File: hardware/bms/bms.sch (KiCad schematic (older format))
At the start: 185 parts

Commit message: fixed power schematics
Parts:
- removed L?: 4.7uH, Inductor_SMD:L_0805_2012Metric, symbol pspice:INDUCTOR
- removed R? (x2): R_Small, Resistor_SMD:R_0603_1608Metric_Pad1.05x0.95mm_HandSolder, symbol Device:R_Small
- added R?: 412K, Resistor_SMD:R_1210_3225Metric_Pad1.42x2.65mm_HandSolder, symbol Device:R
- added R?: 200K, Resistor_SMD:R_1210_3225Metric_Pad1.42x2.65mm_HandSolder, symbol Device:R
- C?: value CAP -> 2.2uF
- C? (x2): value C -> 100nF
- C?: value CP1 -> 22uF
- C?: value C -> 2.2uF
- C? (x2): value C -> 2.2nF
- C?: value C -> 100pF
- C?: value C -> 47uF
- L?: value 47uH -> 68uH
- R?: value 100K -> 82.5K
- R?: value R_Small -> 562K
- R?: value R_Small -> 174K
- R?: value R_Small -> 100K
- U?: value TPS560430 -> TPS560430x3F
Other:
- moved on the sheet: C?, D?, L?, Q?, R?

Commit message: Added On/Off control button
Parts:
- removed C?: 47uF, Capacitor_SMD:C_0603_1608Metric_Pad1.05x0.95mm_HandSolder, symbol Device:C
- removed J? (x4): Conn_01x02, symbol BMS:Conn_01x02
- removed JP?: PackLoad+, symbol BMS:JUMPER
- added C?: 47uF, Capacitor_Tantalum_SMD:CP_EIA-3528-21_Kemet-B, symbol Device:CP1
- added C?: 0.1uF, Capacitor_SMD:C_0603_1608Metric_Pad1.05x0.95mm_HandSolder, symbol Device:C
- added J? (x2): Conn_01x03, symbol Connector_Generic:Conn_01x03
- added JP?: Load On/Off, symbol BMS:JUMPER
- added R?: 10K, Resistor_SMD:R_0603_1608Metric_Pad1.05x0.95mm_HandSolder, symbol Device:R_Small
- added SW?: On/Off, symbol Switch:SW_Push
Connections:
- wire segments 657 -> 666
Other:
- note added: "Pack charging"
- note added: "Pack discharging"
- note added: "Series stacking connectors"
- moved on the sheet: C?, J?, JP?, R?

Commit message: added required provisions
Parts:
- removed J?: Conn_01x06, symbol BMS:Conn_01x06
- removed SW?: On/Off, symbol Switch:SW_Push
- added J?: Conn_01x08, symbol Connector_Generic:Conn_01x08
- added JP?: WakeUp, symbol BMS:JUMPER
- added R? (x4): 10K, Resistor_SMD:R_0603_1608Metric_Pad1.05x0.95mm_HandSolder, symbol Device:R_Small
- added R?: 20K, Resistor_SMD:R_0603_1608Metric_Pad1.05x0.95mm_HandSolder, symbol Device:R_Small
- added SW?: SW_DIP_x03, symbol Switch:SW_DIP_x03
- JP?: value Load On/Off -> Load_On/Off
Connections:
- net labels added: ADC, CFG_ID
- net labels removed: PACK_ID
- wire segments 666 -> 690
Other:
- note added: "CFG_ID ADC"
- note added: "Note: LM5164DDAR has limit of 100V input\nin case the pack voltage exceeds 100V then \na provision is provided with external 5V (+5VF) input\nto wakeup the stm32 if it is powered down due to\nlow Battery"
- note added: "Note:\n1) Load_On/Off is of 10A 100VDC rating\n2) Load_On/Off and wakeup connector \n connects to a panel mounted DPDT switch"
- note removed: "PACK ID ADC"
- moved on the sheet: J?, JP?, R?

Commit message: added bypass link for 3V3 power
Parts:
- added JP?: PWR_3V3_ON, symbol BMS:JUMPER
- JP? (x6): symbol bms-rescue:JUMPER-BMS -> bms-rescue:JUMPER-BMS-bms-rescue
- Q? (x5): symbol bms-rescue:Q_PMOS_GSD-BMS -> bms-rescue:Q_PMOS_GSD-BMS-bms-rescue
- U?: symbol bms-rescue:LSI94202-BMS -> bms-rescue:LSI94202-BMS-bms-rescue
- U?: symbol bms-rescue:TPS560430-BMS -> bms-rescue:TPS560430-BMS-bms-rescue
- U?: symbol bms-rescue:USBLC6-2SC6-BMS -> bms-rescue:USBLC6-2SC6-BMS-bms-rescue
- Y?: symbol bms-rescue:Crystal-BMS -> bms-rescue:Crystal-BMS-bms-rescue
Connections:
- wire segments 690 -> 691
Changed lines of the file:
@@
 $EndDescr
 $Comp
-L bms-rescue:LSI94202-BMS U?
+L bms-rescue:LSI94202-BMS-bms-rescue U?
 U 1 1 5E42CB2D
 P 13000 5600
@@
 OSC_OUT
 $Comp
-L bms-rescue:TPS560430-BMS U?
+L bms-rescue:TPS560430-BMS-bms-rescue U?
 U 1 1 5E454D22
 P 3100 1350
@@
 	1400 6950 1750 6950
 $Comp
-L bms-rescue:USBLC6-2SC6-BMS U?
+L bms-rescue:USBLC6-2SC6-BMS-bms-rescue U?
 U 1 1 5E4A89B6
 P 1700 10300
@@
 	4750 10700 4750 10600
 $Comp
-L bms-rescue:Crystal-BMS Y?
+L bms-rescue:Crystal-BMS-bms-rescue Y?
 U 1 1 5E60121F
 P 2250 4300
@@
 $EndComp
 $Comp
-L bms-rescue:JUMPER-BMS JP?
+L bms-rescue:JUMPER-BMS-bms-rescue JP?
 U 1 1 5E9F8394
 P 4250 9050
@@
 	4850 9050 4850 9100
 $Comp
-L bms-rescue:Q_PMOS_GSD-BMS Q?
+L bms-rescue:Q_PMOS_GSD-BMS-bms-rescue Q?
 U 1 1 5EA725A8
 P 9000 1150
@@
 	8900 1750 8900 1700
 $Comp
-L bms-rescue:Q_PMOS_GSD-BMS Q?
+L bms-rescue:Q_PMOS_GSD-BMS-bms-rescue Q?
 U 1 1 5EC5A053
 P 10750 1150
@@
 	10650 1750 10650 1700
 $Comp
-L bms-rescue:Q_PMOS_GSD-BMS Q?
+L bms-rescue:Q_PMOS_GSD-BMS-bms-rescue Q?
 U 1 1 5EC68673
 P 12600 1150
@@
 $EndComp
 $Comp
-L bms-rescue:JUMPER-BMS JP?
+L bms-rescue:JUMPER-BMS-bms-rescue JP?
 U 1 1 5E474F4B
 P 9100 3550
@@
 $EndComp
 $Comp
-L bms-rescue:JUMPER-BMS JP?
+L bms-rescue:JUMPER-BMS-bms-rescue JP?
 U 1 1 5E475BC8
 P 9100 3700
@@
 $EndComp
 $Comp
-L bms-rescue:JUMPER-BMS JP?
+L bms-rescue:JUMPER-BMS-bms-rescue JP?
 U 1 1 5E4767E4
 P 9100 3850
@@
 C3
 $Comp
-L bms-rescue:JUMPER-BMS JP?
+L bms-rescue:JUMPER-BMS-bms-rescue JP?
 U 1 1 5E476B2E
 P 9100 4000
@@
 $EndComp
 $Comp
-L bms-rescue:JUMPER-BMS JP?
+L bms-rescue:JUMPER-BMS-bms-rescue JP?
 U 1 1 5E476E99
 P 9100 4150
@@
 	12250 7800 12000 7800
 $Comp
-L bms-rescue:Q_PMOS_GSD-BMS Q?
+L bms-rescue:Q_PMOS_GSD-BMS-bms-rescue Q?
 U 1 1 5FFFA185
 P 9750 7900
@@
 	5450 6550 5450 6500
 $Comp
-L bms-rescue:Q_PMOS_GSD-BMS Q?
+L bms-rescue:Q_PMOS_GSD-BMS-bms-rescue Q?
 U 1 1 5E4FE228
 P 10650 9550
@@
 	5500 9600 5500 9500
 Wire Notes Line
-	8000 11050 8000 7450
+	7500 11050 7500 7450
 Wire Notes Line
-	8000 11050 11450 11050
-Text Notes 6800 5900 0    50   ~ 0
-Populate for Bottom Node only
+	7500 11050 11450 11050
 Text GLabel 10050 10400 0    50   Input ~ 0
 PWR-
@@
 	1    0    0    -1
 $EndComp
-Text GLabel 6950 6300 0    50   Input ~ 0
+Text GLabel 6400 6300 0    50   Input ~ 0
 PWR+
 Text GLabel 6950 7100 0    50   Input ~ 0
@@
 Wire Wire Line
 	7100 6550 7100 6300
-Connection ~ 7100 6300
-Wire Wire Line
-	7100 6300 6950 6300
 Wire Wire Line
 	7100 6850 7100 7100
@@
 	10750 6150 10750 6300
 Connection ~ 10200 6150
-Wire Wire Line
-	11000 6150 10750 6150
 Connection ~ 10750 6150
 $Comp
@@
 Wire Wire Line
 	4900 5900 5000 5900
-Connection ~ 11000 6150
 Wire Wire Line
 	8550 9800 8600 9800
 Text GLabel 8550 9800 0    50   Input ~ 0
 LOAD-
-Text Notes 7700 4500 0    50   ~ 0
+Text Notes 7700 4500 0    50   ~ 10
 Populate for TOP Node only
 Text GLabel 8550 9350 0    50   Input ~ 0
@@
 $EndComp
 Wire Notes Line
-	8000 7450 6600 7450
+	7500 7450 6100 7450
 Wire Notes Line
-	6600 5800 11450 5800
+	6100 5800 11450 5800
 Wire Notes Line
-	6600 5800 6600 7450
+	6100 5800 6100 7450
 Wire Notes Line
 	11450 5800 11450 11050
@@
 Wire Wire Line
 	1300 3400 1450 3400
-Text Notes 8150 7550 0    50   ~ 0
+Text Notes 7600 7550 0    50   ~ 0
 Note: LM5164DDAR has limit of 100V input\nin case the pack voltage exceeds 100V then \na provision is provided with external 5V (+5VF) input\nto wakeup the stm32 if it is powered down due to\nlow Battery
+Connection ~ 11000 6150
+Wire Wire Line
+	11000 6150 10750 6150
+$Comp
+L BMS:JUMPER JP?
+U 1 1 5E58BBD4
+P 6750 6300
+F 0 "JP?" H 6750 6564 50  0000 C CNN
+F 1 "PWR_3V3_ON" H 6750 6473 50  0000 C CNN
+F 2 "" H 6750 6300 50  0000 C CNN
+F 3 "" H 6750 6300 50  0000 C CNN
+	1    6750 6300
+	1    0    0    -1
+$EndComp
+Wire Wire Line
+	6400 6300 6450 6300
+Wire Wire Line
+	7050 6300 7100 6300
+Connection ~ 7100 6300
+Text Notes 6150 5900 0    50   ~ 10
+Populate for Bottom Node only
 $EndSCHEMATC

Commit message: started adding footprint
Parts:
- removed JP? (x2): JUMPER3, symbol BMS:JUMPER3
- removed Q? (x3): Q_NMOS_DGS, symbol Device:Q_NMOS_DGS
- added D?: 100V, Diode_SMD:D_MELF_Handsoldering, symbol Device:D_Zener_Small
- added Q? (x3): IRF540N, Package_TO_SOT_SMD:TO-263-2, symbol Transistor_FET:IRF540N
- added R?: 1K, Resistor_SMD:R_1206_3216Metric_Pad1.42x1.75mm_HandSolder, symbol Device:R_Small
- added R? (x4): 0E, Resistor_SMD:R_0603_1608Metric_Pad1.05x0.95mm_HandSolder, symbol Device:R_Small
- L?: footprint (none) -> Inductor_SMD:L_Wuerth_HCI-1365
- Q? (x2): footprint (none) -> Package_TO_SOT_SMD:TO-252-3_TabPin2
- U?: value LM5164 -> LM5164DDAR
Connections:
- net +BATT: now also Q?.3 (S)
- net 485_A: now also R?.2
- net 485_B: now also R?.2
- net CANH: now also R?.1
- net CANL: now also R?.1
- net CHG: now also Q?.2 (D)
- net Data_H_A: now also R?.1, R?.2
- net Data_L_B: now also R?.1, R?.2
- net LOAD: now also Q?.2 (D)
- net PWR-: now also D?.2 (A)
- net VDD: now also Q?.3 (S), Q?.3 (S)
- net at C?.1, JP?.2, U?.2 (VIN)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: now also R?.2
- net at R?.1, R?.1: now also Q?.1 (G) (x3)
- net at R?.2: now also Q?.2 (D)
- new net: D?.1 (K), R?.1
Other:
- moved on the sheet: C?, JP?, R?

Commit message: corrected and added footprints
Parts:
- removed JP?: BOOT_SEL, symbol bms-rescue:JUMPER-BMS-bms-rescue
- removed Q? (x3): Q_PMOS_GSD, symbol bms-rescue:Q_PMOS_GSD-BMS-bms-rescue
- removed R?: 20K, Resistor_SMD:R_0603_1608Metric_Pad1.05x0.95mm_HandSolder, symbol Device:R_Small
- added Q10, Q2, Q9: ZXMP4A16G, Package_TO_SOT_SMD:SOT-223-3_TabPin2, symbol Transistor_FET:ZXMP4A16G
- FB1: renamed from FB?; footprint (none) -> Inductor_SMD:L_0805_2012Metric_Pad1.15x1.40mm_HandSolder
- J1: renamed from J?; footprint (none) -> Connector_PinHeader_1.00mm:PinHeader_1x08_P1.00mm_Vertical
- J10, J11, J12, J9: renamed from J?; footprint (none) -> TerminalBlock:TerminalBlock_bornier-2_P5.08mm
- J14: renamed from J?; footprint (none) -> Connector_PinSocket_2.54mm:PinSocket_1x02_P2.54mm_Vertical
- J15: renamed from J?; footprint (none) -> Connector_Molex:Molex_KK-396_A-41791-0002_1x02_P3.96mm_Vertical
- J2, J5, J6: renamed from J?; footprint (none) -> Connector_Molex:Molex_KK-254_AE-6410-04A_1x04_P2.54mm_Vertical
- J3: renamed from J?; footprint (none) -> Connector_USB:USB_Micro-B_Molex-105017-0001
- J4: renamed from J?; footprint (none) -> Connector_Molex:Molex_KK-254_AE-6410-05A_1x05_P2.54mm_Vertical
- J7, J8: renamed from J?; footprint (none) -> TerminalBlock:TerminalBlock_bornier-3_P5.08mm
- JP1, JP10, JP11, JP2, JP3, JP4, JP5, JP6, JP7, JP8: renamed from JP?; footprint (none) -> Connector_PinHeader_2.54mm:PinHeader_1x02_P2.54mm_Vertical
- JP9: renamed from JP?; value PackCHG -> Connector_PinHeader_2.54mm:PinHeader_1x02_P2.54mm_Vertical; footprint (none) -> Connector_PinHeader_2.54mm:PinHeader_1x02_P2.54mm_Vertical
- SW1: renamed from SW?; footprint (none) -> Button_Switch_SMD:SW_DIP_SPSTx03_Slide_6.7x9.18mm_W6.73mm_P2.54mm_LowProfile_JPin
- TP1, TP2, TP3, TP4, TP5: renamed from TP?; footprint (none) -> TestPoint:TestPoint_Pad_D1.5mm
- U4: renamed from U?; footprint (none) -> Package_SO:SOIC-8-N7_3.9x4.9mm_P1.27mm
- U5: renamed from U?; footprint (none) -> Package_SO:SOIC-8_3.9x4.9mm_P1.27mm
- U6: renamed from U?; footprint Package_SO:SOIC-8-1EP_3.9x4.9mm_P1.27mm_EP2.95x4.9mm_Mask2.71x3.4mm_ThermalVias -> Package_SO:SOIC-8-1EP_3.9x4.9mm_P1.27mm_EP2.514x3.2mm_ThermalVias
- U7: renamed from U?; footprint (none) -> Package_DFN_QFN:QFN-48-1EP_6x6mm_P0.4mm_EP4.66x4.66mm_ThermalVias
- Y1: renamed from Y?; footprint (none) -> Crystal:Crystal_SMD_HC49-SD_HandSoldering
- gave numbers to parts that had none: 154
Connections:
- net BOOT0: now also SW1.4
- net C1: now also Q13.3 (D); no longer Q13.2 (S)
- net C1-: now also Q16.3 (D); no longer Q16.2 (S)
- net C2: now also Q8.3 (D); no longer Q8.2 (S)
- net C3: now also Q3.3 (D); no longer Q3.2 (S)
- net C4: now also Q15.3 (D); no longer Q15.2 (S)
- net C6: now also Q10.3 (S)
- net C7: now also Q9.3 (S)
- net C8: now also Q2.3 (S)
- net CANH: no longer R25.2
- net CANL: no longer R25.1
- net CFG_ID: no longer R24.2
- net Data_H_A: now also R25.2
- net Data_L_B: now also R25.1
- net GND: now also R24.1; no longer SW1.3
- net at R33.1, R38.2: now also Q2.1 (G)
- net at R29.2: now also Q2.2 (D)
- net at R52.1, R57.2: now also Q9.1 (G)
- net at R48.2: now also Q9.2 (D)
- net at R65.1, R69.2: now also Q10.1 (G)
- net at R61.2: now also Q10.2 (D)
- net at R73.1: now also Q15.2 (S); no longer Q15.3 (D)
- net at R30.1: now also Q3.2 (S); no longer Q3.3 (D)
- net at R47.1: now also Q8.2 (S); no longer Q8.3 (D)
- net at R62.1: now also Q13.2 (S); no longer Q13.3 (D)
- net at R74.1: now also Q16.2 (S); no longer Q16.3 (D)
- new net: R24.2, SW1.3
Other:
- note added: "BOOT_SEL"
- moved on the sheet: R24, SW1

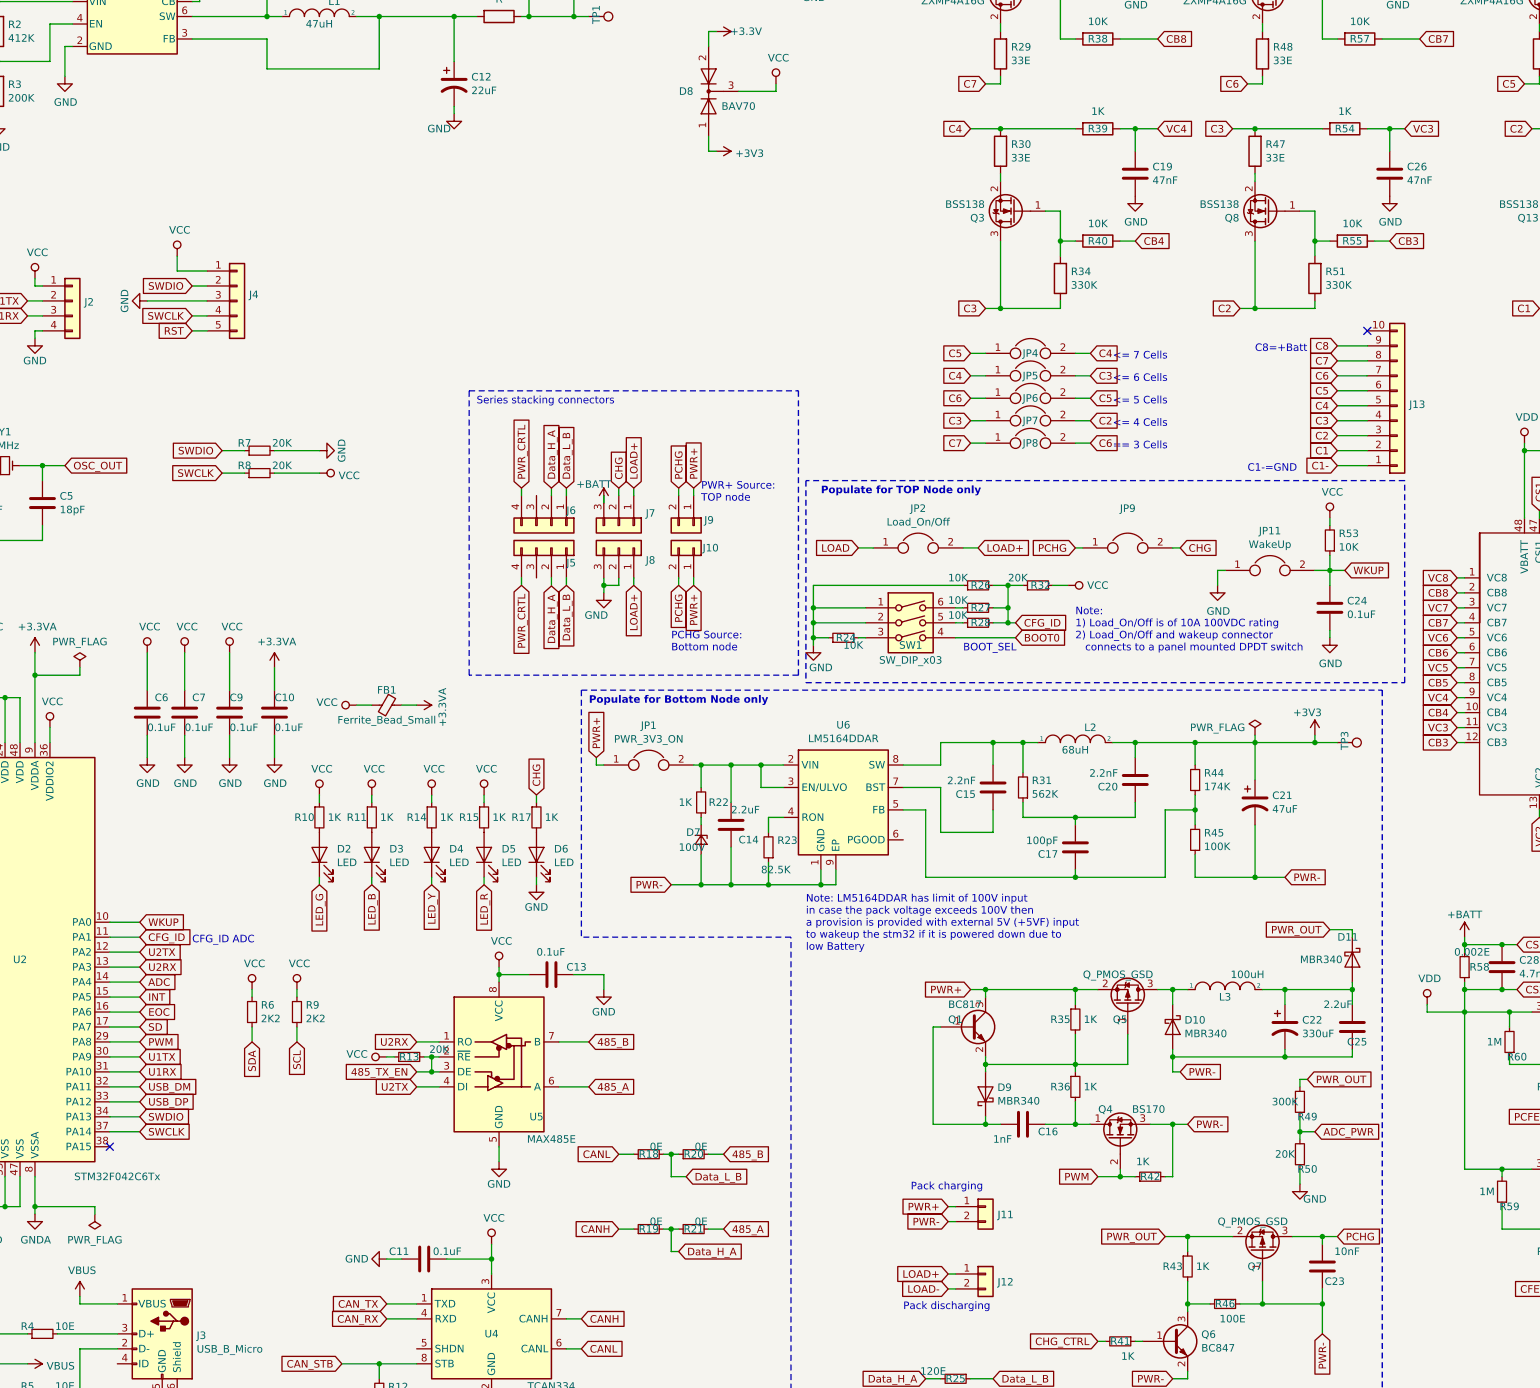
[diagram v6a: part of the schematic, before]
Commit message: fixed footprints
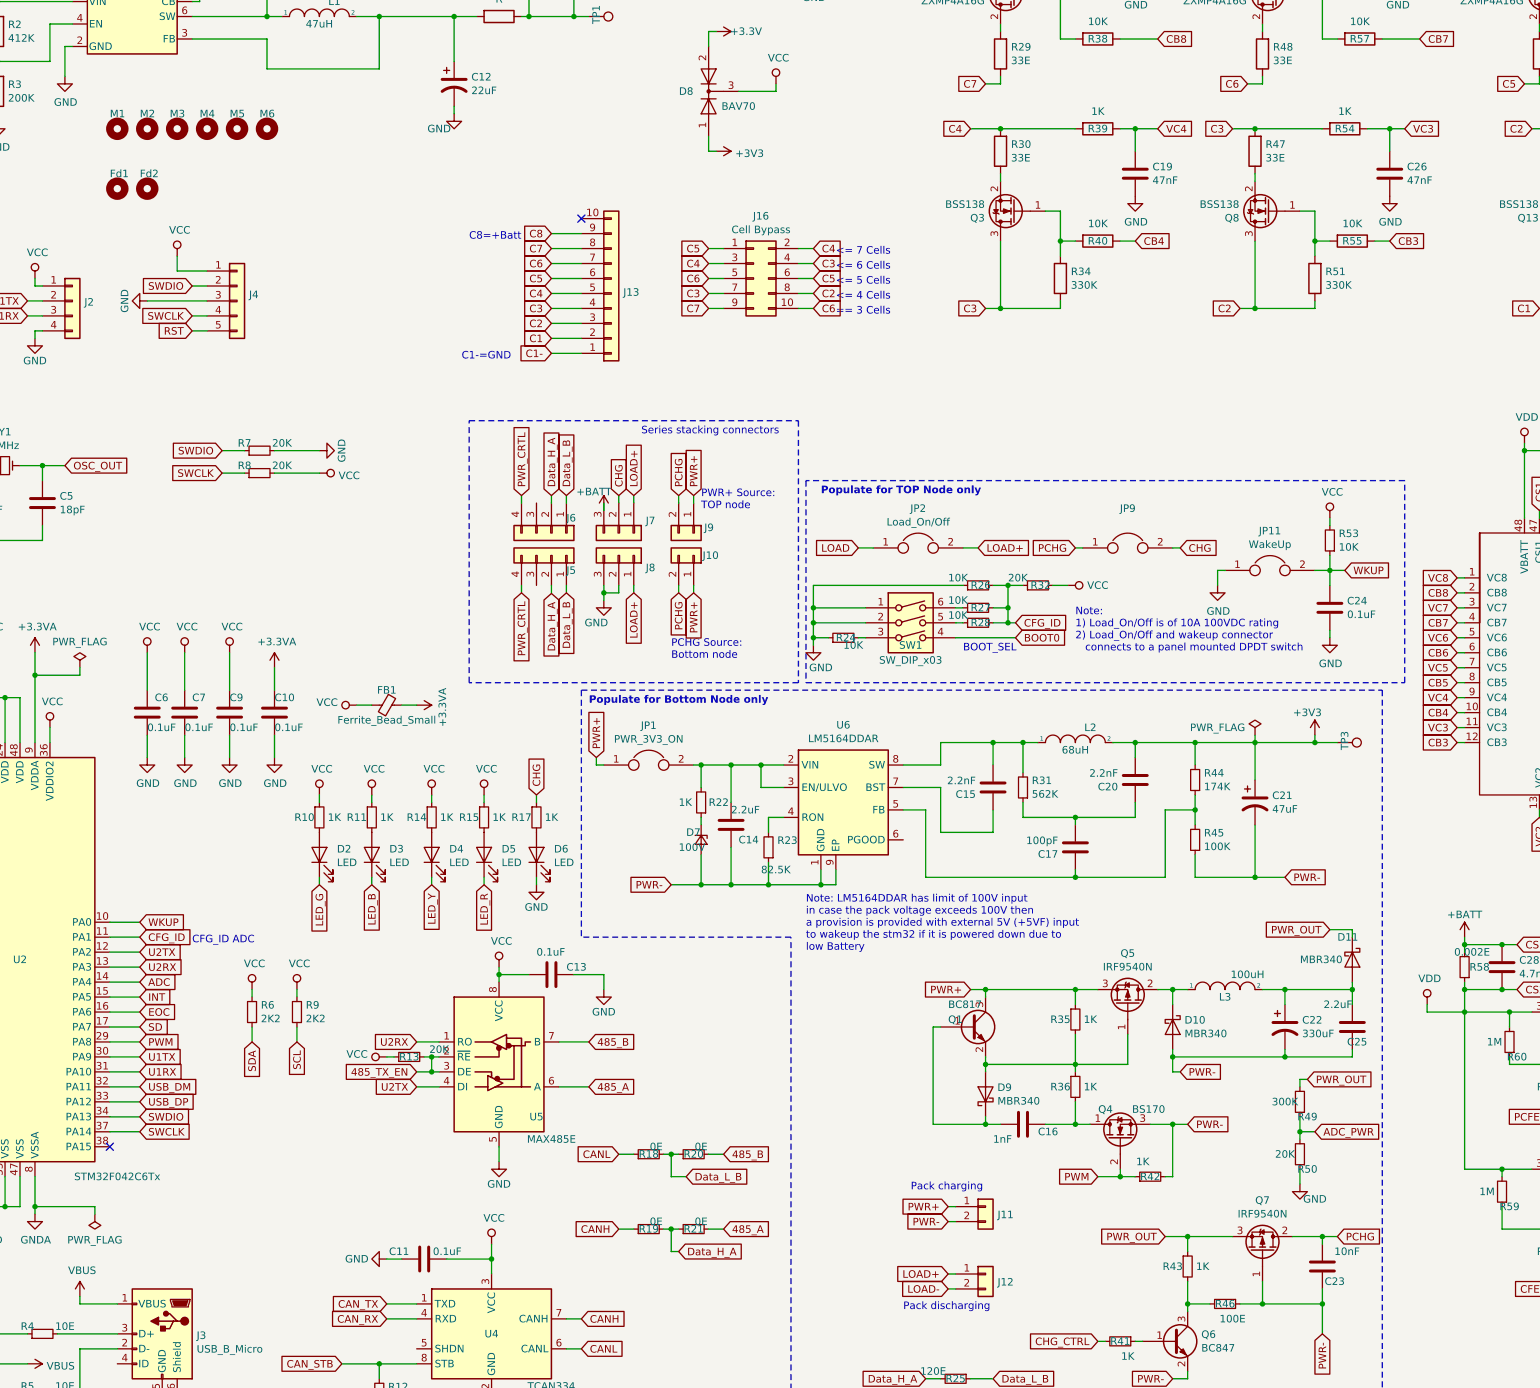
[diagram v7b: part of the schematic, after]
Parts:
- removed JP4, JP5, JP6, JP7, JP8: JUMPER, Connector_PinHeader_2.54mm:PinHeader_1x02_P2.54mm_Vertical, symbol bms-rescue:JUMPER-BMS-bms-rescue
- removed Q5, Q7: Q_PMOS_GSD, Package_TO_SOT_SMD:TO-252-3_TabPin2, symbol bms-rescue:Q_PMOS_GSD-BMS-bms-rescue
- added Fd1, Fd2: MountingHole, Fiducial:Fiducial_1mm_Mask2mm, symbol Mechanical:MountingHole
- added J16: Cell Bypass, Connector_PinHeader_2.54mm:PinHeader_2x05_P2.54mm_Vertical, symbol Connector_Generic:Conn_02x05_Odd_Even
- added M1, M2, M3, M4, M5, M6: MountingHole, MountingHole:MountingHole_3.2mm_M3_Pad, symbol Mechanical:MountingHole
- added Q5, Q7: IRF9540N, Package_TO_SOT_THT:TO-220-3_Vertical, symbol Transistor_FET:IRF9540N
- J13: footprint (none) -> Connector_Molex:Molex_KK-254_AE-6410-10A_1x10_P2.54mm_Vertical
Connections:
- net C2: now also J16.8 (Pin_8)
- net C3: now also J16.4 (Pin_4), J16.7 (Pin_7)
- net C4: now also J16.2 (Pin_2), J16.3 (Pin_3)
- net C5: now also J16.1 (Pin_1), J16.6 (Pin_6)
- net C6: now also J16.10 (Pin_10), J16.5 (Pin_5)
- net C7: now also J16.9 (Pin_9)
- net PCHG: now also Q7.2 (D)
- net PWR+: now also Q5.3 (S)
- net PWR-: now also Q7.1 (G)
- net PWR_OUT: now also Q7.3 (S)
- net at D9.2 (A), Q1.2 (E), R35.2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: now also Q5.1 (G)
- net at D10.1 (K), L3.1: now also Q5.2 (D)
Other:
- moved on the sheet: J10, J13, J5, J6, J7, J8, J9
